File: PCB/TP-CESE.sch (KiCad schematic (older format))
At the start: 27 parts, among them J1 Conn_01x04_Female, J2 Conn_02x02_Odd_Even, Q1 IRF540N, Q2 IRF540N, Q3 IRF540N, Q4 IRF540N, U1 4N25, U2 4N25, U3 4N25, U4 4N25

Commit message: Agrego libreria poncho de edu-ciaa y hojas de datos
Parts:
- removed J1: Conn_01x04_Female, symbol Connector:Conn_01x04_Female
- removed J2: Conn_02x02_Odd_Even, Connector_PinSocket_2.54mm:PinSocket_2x02_P2.54mm_Vertical, symbol Connector_Generic:Conn_02x02_Odd_Even
- added J1: Screw_Terminal_01x04, symbol Connector:Screw_Terminal_01x04
- added J3: Screw_Terminal_01x02, symbol Connector:Screw_Terminal_01x02
- added XA? (x2): Conn_Poncho2P_2x_20x2, symbol Poncho_Esqueleto:Conn_Poncho2P_2x_20x2
- gave numbers to parts that had none: 1
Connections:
- wire segments 71 -> 87
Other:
- note added: "Alimentacion fuente de alimentacion\ndiferente de Edu-Ciaa \nTension de alimentacion: 5Volts /3 Amp\n"
- moved on the sheet: Q1, Q2, Q3, Q4, R1, R10, R11, R12, R13, R14, R15, R16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

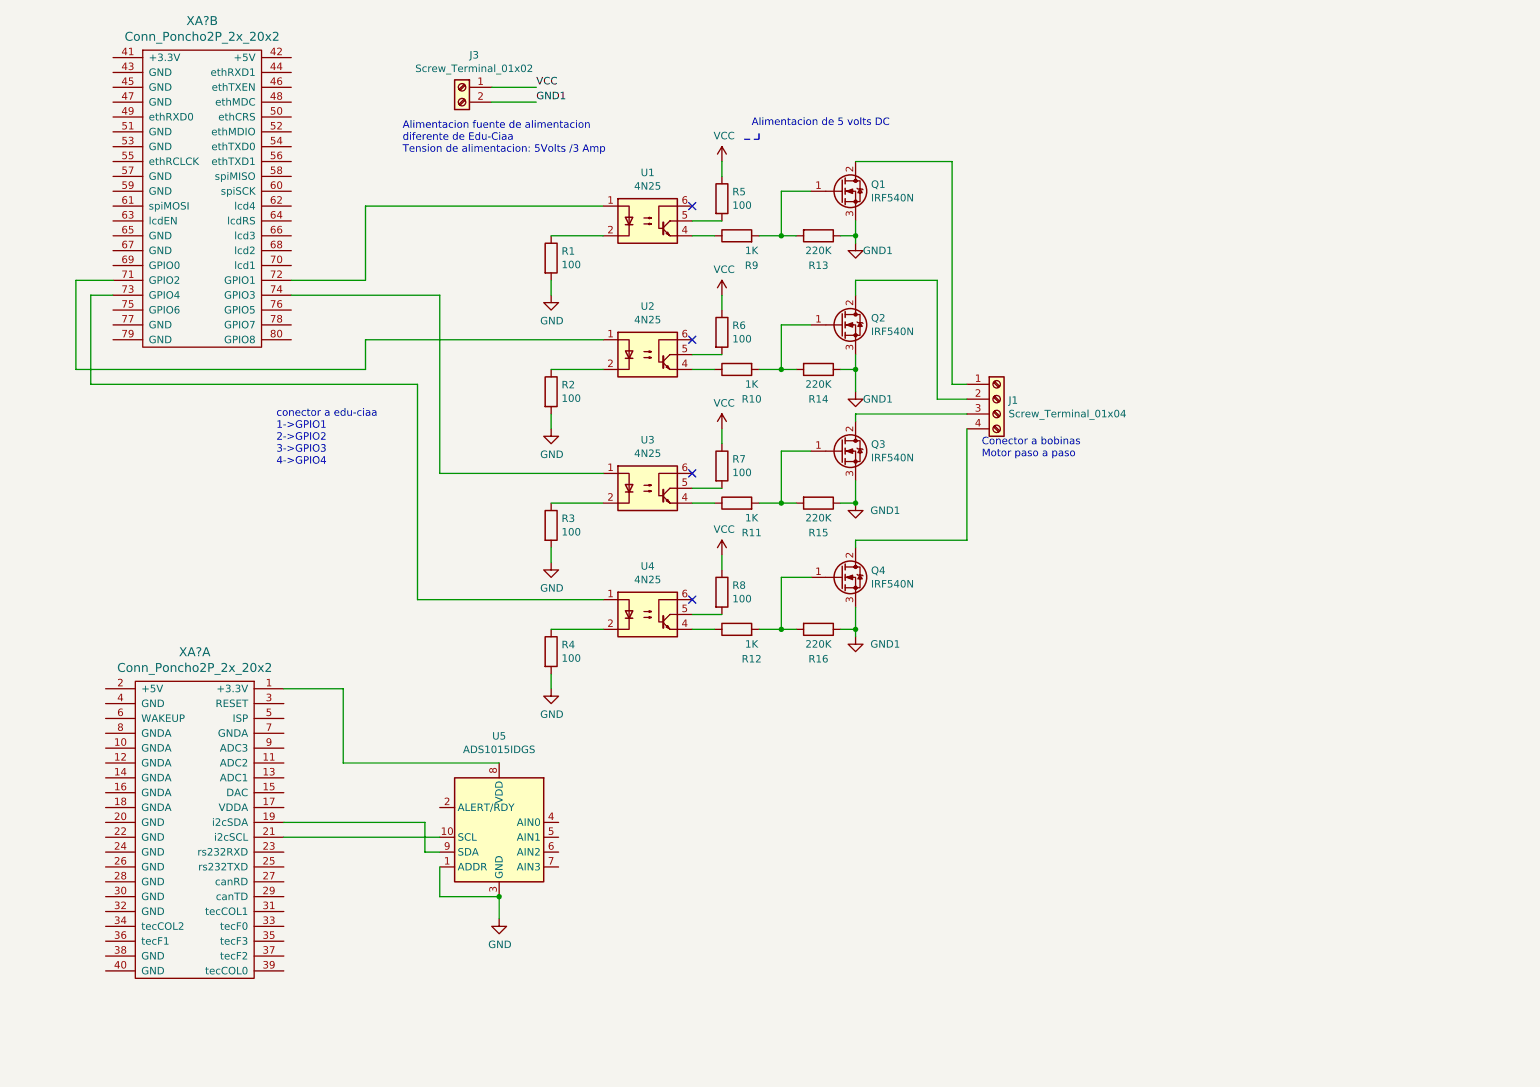
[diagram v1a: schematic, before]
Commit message: Conexiones, diodos de protecccion
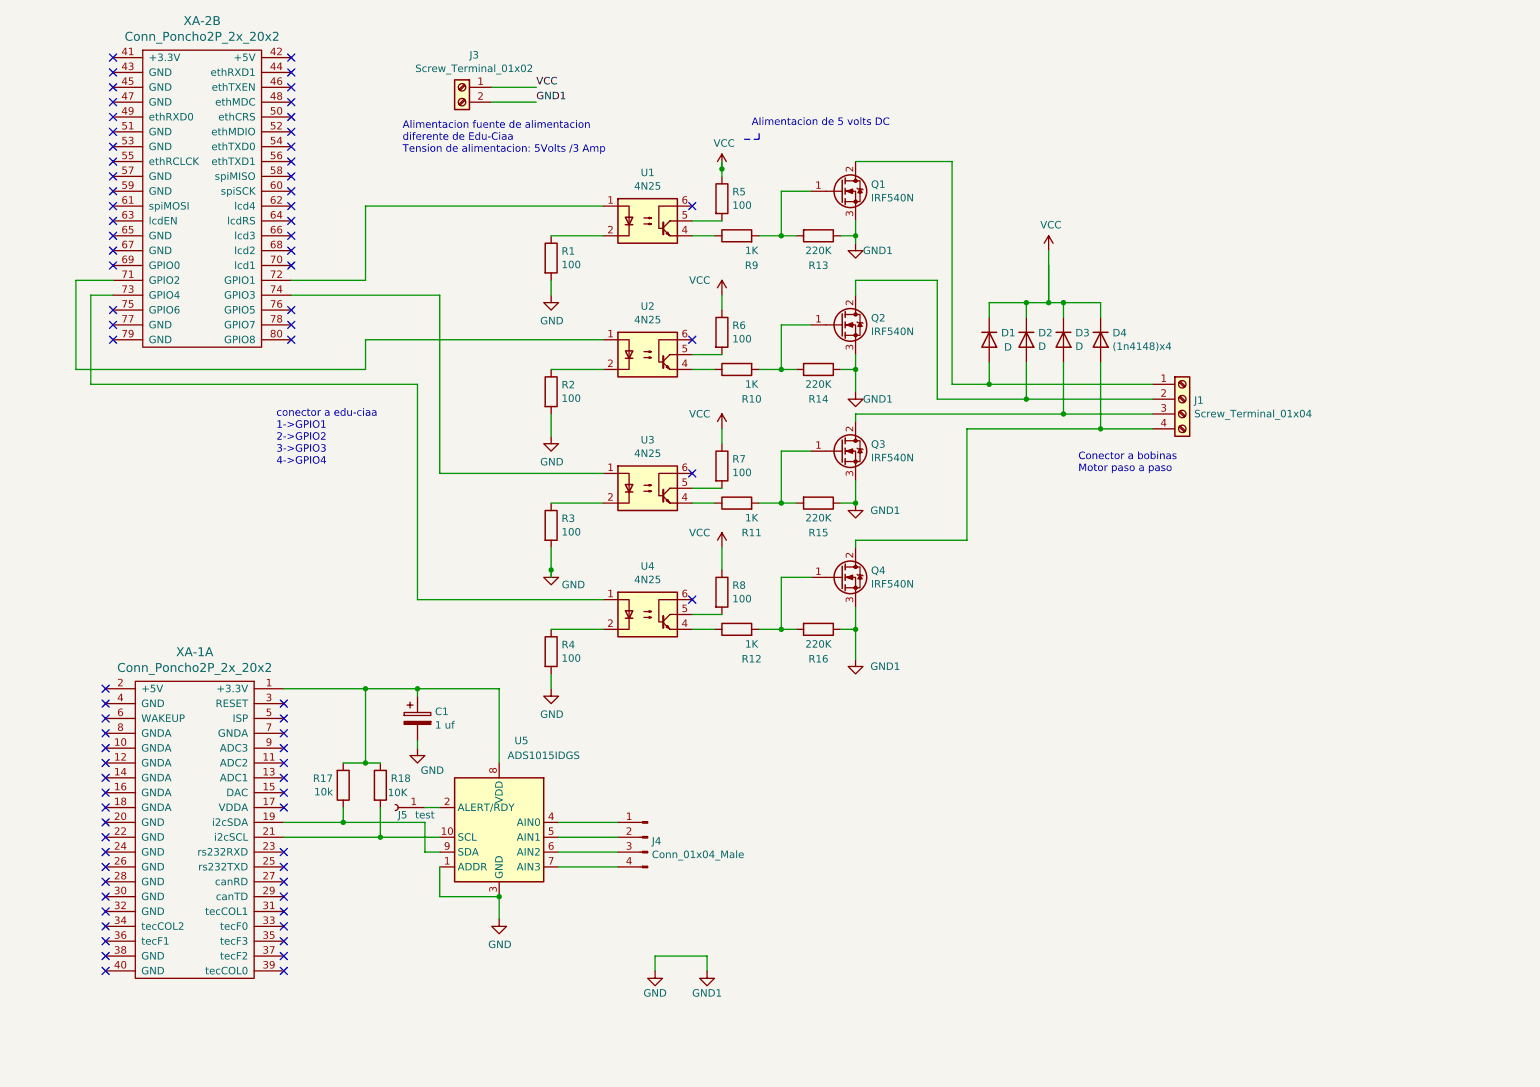
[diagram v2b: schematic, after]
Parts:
- added C1: 1 uf, symbol Device:CP
- added D1, D2, D3: D, symbol Device:D
- added D4: (1n4148)x4, symbol Device:D
- added J4: Conn_01x04_Male, symbol Connector:Conn_01x04_Male
- added J5: test, symbol Connector:Conn_01x01_Female
- added R17: 10k, symbol Device:R
- added R18: 10K, symbol Device:R
- gave numbers to parts that had none: 2
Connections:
- net GND1 is gone; now on net GND: J3.2 (Pin_2), Q1.3 (S), Q2.3 (S), Q3.3 (S), Q4.3 (S), R13.1, R14.1, R15.1, R16.1
- net GND: now also C1.2
- net VCC: now also D1.1 (K), D2.1 (K), D3.1 (K), D4.1 (K)
- net at J1.1 (Pin_1), Q1.2 (D): now also D1.2 (A)
- net at J1.2 (Pin_2), Q2.2 (D): now also D2.2 (A)
- net at J1.3 (Pin_3), Q3.2 (D): now also D3.2 (A)
- net at J1.4 (Pin_4), Q4.2 (D): now also D4.2 (A)
- net at U5.8 (VDD), XA-1.1 (+3.3V): now also C1.1, R17.2, R18.1
- net at U5.9 (SDA), XA-1.19 (i2cSDA): now also R17.1
- net at U5.10 (SCL), XA-1.21 (i2cSCL): now also R18.2
- net at U5.2 (ALERT/RDY): now also J5.1 (Pin_1)
- net at U5.4 (AIN0): now also J4.1 (Pin_1)
- net at U5.5 (AIN1): now also J4.2 (Pin_2)
- net at U5.6 (AIN2): now also J4.3 (Pin_3)
- net at U5.7 (AIN3): now also J4.4 (Pin_4)
- no-connect marks 4 -> 77
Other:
- moved on the sheet: J1

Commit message: agrego huellas, hojas de datos de diodo y tabla de potencia de resistencia smd
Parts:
- C1: footprint (none) -> Capacitor_SMD:CP_Elec_4x5.4
- D1, D2, D3, D4: footprint (none) -> Diode_THT:D_5W_P10.16mm_Horizontal
- J1: footprint (none) -> TerminalBlock_Phoenix:TerminalBlock_Phoenix_MKDS-1,5-4-5.08_1x04_P5.08mm_Horizontal
- J3: footprint (none) -> TerminalBlock_Phoenix:TerminalBlock_Phoenix_MKDS-1,5-2-5.08_1x02_P5.08mm_Horizontal
- J4: footprint (none) -> Connector_PinHeader_2.00mm:PinHeader_1x04_P2.00mm_Vertical
- J5: footprint (none) -> Connector_PinHeader_2.00mm:PinHeader_1x01_P2.00mm_Vertical
- Q1, Q2, Q3, Q4: footprint Package_TO_SOT_THT:TO-220-3_Vertical -> Package_TO_SOT_THT:TO-262-3_Vertical
- R1, R2, R3, R4: footprint (none) -> Resistor_SMD:R_2010_5025Metric_Pad1.52x2.65mm_HandSolder
- R10, R11, R12, R5, R6, R7, R8, R9: footprint (none) -> Resistor_SMD:R_2512_6332Metric_Pad1.52x3.35mm_HandSolder
- R13, R14, R15, R16, R17, R18: footprint (none) -> Resistor_SMD:R_1210_3225Metric
- XA-1, XA-2: footprint (none) -> Poncho_Esqueleto:Conn_Poncho_Chico
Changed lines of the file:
@@
 F 0 "R1" H 4320 2196 50  0000 L CNN
 F 1 "100" H 4320 2105 50  0000 L CNN
-F 2 "" V 4180 2150 50  0001 C CNN
+F 2 "Resistor_SMD:R_2010_5025Metric_Pad1.52x2.65mm_HandSolder" V 4180 2150 50  0001 C CNN
 F 3 "~" H 4250 2150 50  0001 C CNN
 	1    4250 2150
@@
 F 0 "R2" H 4320 3096 50  0000 L CNN
 F 1 "100" H 4320 3005 50  0000 L CNN
-F 2 "" V 4180 3050 50  0001 C CNN
+F 2 "Resistor_SMD:R_2010_5025Metric_Pad1.52x2.65mm_HandSolder" V 4180 3050 50  0001 C CNN
 F 3 "~" H 4250 3050 50  0001 C CNN
 	1    4250 3050
@@
 F 0 "R3" H 4320 3996 50  0000 L CNN
 F 1 "100" H 4320 3905 50  0000 L CNN
-F 2 "" V 4180 3950 50  0001 C CNN
+F 2 "Resistor_SMD:R_2010_5025Metric_Pad1.52x2.65mm_HandSolder" V 4180 3950 50  0001 C CNN
 F 3 "~" H 4250 3950 50  0001 C CNN
 	1    4250 3950
@@
 F 0 "R4" H 4320 4846 50  0000 L CNN
 F 1 "100" H 4320 4755 50  0000 L CNN
-F 2 "" V 4180 4800 50  0001 C CNN
+F 2 "Resistor_SMD:R_2010_5025Metric_Pad1.52x2.65mm_HandSolder" V 4180 4800 50  0001 C CNN
 F 3 "~" H 4250 4800 50  0001 C CNN
 	1    4250 4800
@@
 F 0 "R5" H 5470 1796 50  0000 L CNN
 F 1 "100" H 5470 1705 50  0000 L CNN
-F 2 "" V 5330 1750 50  0001 C CNN
+F 2 "Resistor_SMD:R_2512_6332Metric_Pad1.52x3.35mm_HandSolder" V 5330 1750 50  0001 C CNN
 F 3 "~" H 5400 1750 50  0001 C CNN
 	1    5400 1750
@@
 F 0 "R6" H 5470 2696 50  0000 L CNN
 F 1 "100" H 5470 2605 50  0000 L CNN
-F 2 "" V 5330 2650 50  0001 C CNN
+F 2 "Resistor_SMD:R_2512_6332Metric_Pad1.52x3.35mm_HandSolder" V 5330 2650 50  0001 C CNN
 F 3 "~" H 5400 2650 50  0001 C CNN
 	1    5400 2650
@@
 F 0 "R7" H 5470 3596 50  0000 L CNN
 F 1 "100" H 5470 3505 50  0000 L CNN
-F 2 "" V 5330 3550 50  0001 C CNN
+F 2 "Resistor_SMD:R_2512_6332Metric_Pad1.52x3.35mm_HandSolder" V 5330 3550 50  0001 C CNN
 F 3 "~" H 5400 3550 50  0001 C CNN
 	1    5400 3550
@@
 F 0 "R8" H 5470 4446 50  0000 L CNN
 F 1 "100" H 5470 4355 50  0000 L CNN
-F 2 "" V 5330 4400 50  0001 C CNN
+F 2 "Resistor_SMD:R_2512_6332Metric_Pad1.52x3.35mm_HandSolder" V 5330 4400 50  0001 C CNN
 F 3 "~" H 5400 4400 50  0001 C CNN
 	1    5400 4400
@@
 F 0 "R9" V 5300 1900 50  0000 C CNN
 F 1 "1K" V 5400 1900 50  0000 C CNN
-F 2 "" V 5430 2000 50  0001 C CNN
+F 2 "Resistor_SMD:R_2512_6332Metric_Pad1.52x3.35mm_HandSolder" V 5430 2000 50  0001 C CNN
 F 3 "~" H 5500 2000 50  0001 C CNN
 	1    5500 2000
@@
 F 0 "R10" V 5700 2800 50  0000 C CNN
 F 1 "1K" V 5600 2800 50  0000 C CNN
-F 2 "" V 5430 2900 50  0001 C CNN
+F 2 "Resistor_SMD:R_2512_6332Metric_Pad1.52x3.35mm_HandSolder" V 5430 2900 50  0001 C CNN
 F 3 "~" H 5500 2900 50  0001 C CNN
 	1    5500 2900
@@
 F 0 "R11" V 5300 3700 50  0000 C CNN
 F 1 "1K" V 5400 3700 50  0000 C CNN
-F 2 "" V 5430 3800 50  0001 C CNN
+F 2 "Resistor_SMD:R_2512_6332Metric_Pad1.52x3.35mm_HandSolder" V 5430 3800 50  0001 C CNN
 F 3 "~" H 5500 3800 50  0001 C CNN
 	1    5500 3800
@@
 F 0 "R12" V 5300 4550 50  0000 C CNN
 F 1 "1K" V 5400 4550 50  0000 C CNN
-F 2 "" V 5430 4650 50  0001 C CNN
+F 2 "Resistor_SMD:R_2512_6332Metric_Pad1.52x3.35mm_HandSolder" V 5430 4650 50  0001 C CNN
 F 3 "~" H 5500 4650 50  0001 C CNN
 	1    5500 4650
@@
 F 0 "R13" V 6250 2000 50  0000 C CNN
 F 1 "220K" V 6150 2000 50  0000 C CNN
-F 2 "" V 5980 2000 50  0001 C CNN
+F 2 "Resistor_SMD:R_1210_3225Metric" V 5980 2000 50  0001 C CNN
 F 3 "~" H 6050 2000 50  0001 C CNN
 	1    6050 2000
@@
 F 0 "R14" V 6250 2900 50  0000 C CNN
 F 1 "220K" V 6150 2900 50  0000 C CNN
-F 2 "" V 5980 2900 50  0001 C CNN
+F 2 "Resistor_SMD:R_1210_3225Metric" V 5980 2900 50  0001 C CNN
 F 3 "~" H 6050 2900 50  0001 C CNN
 	1    6050 2900
@@
 F 0 "R15" V 6250 3800 50  0000 C CNN
 F 1 "220K" V 6150 3800 50  0000 C CNN
-F 2 "" V 5980 3800 50  0001 C CNN
+F 2 "Resistor_SMD:R_1210_3225Metric" V 5980 3800 50  0001 C CNN
 F 3 "~" H 6050 3800 50  0001 C CNN
 	1    6050 3800
@@
 F 0 "R16" V 6250 4650 50  0000 C CNN
 F 1 "220K" V 6150 4650 50  0000 C CNN
-F 2 "" V 5980 4650 50  0001 C CNN
+F 2 "Resistor_SMD:R_1210_3225Metric" V 5980 4650 50  0001 C CNN
 F 3 "~" H 6050 4650 50  0001 C CNN
 	1    6050 4650
@@
 F 0 "Q1" H 6404 1746 50  0000 L CNN
 F 1 "IRF540N" H 6404 1655 50  0000 L CNN
-F 2 "Package_TO_SOT_THT:TO-220-3_Vertical" H 6450 1625 50  0001 L CIN
+F 2 "Package_TO_SOT_THT:TO-262-3_Vertical" H 6450 1625 50  0001 L CIN
 F 3 "http://www.irf.com/product-info/datasheets/data/irf540n.pdf" H 6200 1700 50  0001 L CNN
 	1    6200 1700
@@
 F 0 "Q2" H 6404 2646 50  0000 L CNN
 F 1 "IRF540N" H 6404 2555 50  0000 L CNN
-F 2 "Package_TO_SOT_THT:TO-220-3_Vertical" H 6450 2525 50  0001 L CIN
+F 2 "Package_TO_SOT_THT:TO-262-3_Vertical" H 6450 2525 50  0001 L CIN
 F 3 "http://www.irf.com/product-info/datasheets/data/irf540n.pdf" H 6200 2600 50  0001 L CNN
 	1    6200 2600
@@
 F 0 "Q3" H 6404 3496 50  0000 L CNN
 F 1 "IRF540N" H 6404 3405 50  0000 L CNN
-F 2 "Package_TO_SOT_THT:TO-220-3_Vertical" H 6450 3375 50  0001 L CIN
+F 2 "Package_TO_SOT_THT:TO-262-3_Vertical" H 6450 3375 50  0001 L CIN
 F 3 "http://www.irf.com/product-info/datasheets/data/irf540n.pdf" H 6200 3450 50  0001 L CNN
 	1    6200 3450
@@
 F 0 "Q4" H 6404 4346 50  0000 L CNN
 F 1 "IRF540N" H 6404 4255 50  0000 L CNN
-F 2 "Package_TO_SOT_THT:TO-220-3_Vertical" H 6450 4225 50  0001 L CIN
+F 2 "Package_TO_SOT_THT:TO-262-3_Vertical" H 6450 4225 50  0001 L CIN
 F 3 "http://www.irf.com/product-info/datasheets/data/irf540n.pdf" H 6200 4300 50  0001 L CNN
 	1    6200 4300
@@
 NoConn ~ 5200 2700
 NoConn ~ 5200 1800
-Text Notes 5600 1350 0    50   ~ 0
-Alimentacion de 5 volts DC \n\n
 Wire Notes Line
 	5550 1350 5650 1350
 Wire Notes Line
 	5650 1350 5650 1300
-Wire Wire Line
-	6300 1500 6950 1500
-Wire Wire Line
-	6950 1500 6950 3000
 Wire Wire Line
 	6300 2400 6300 2300
@@
 F 0 "J1" H 8580 3092 50  0000 L CNN
 F 1 "Screw_Terminal_01x04" H 8580 3001 50  0000 L CNN
-F 2 "" H 8500 3100 50  0001 C CNN
+F 2 "TerminalBlock_Phoenix:TerminalBlock_Phoenix_MKDS-1,5-4-5.08_1x04_P5.08mm_Horizontal" H 8500 3100 50  0001 C CNN
 F 3 "~" H 8500 3100 50  0001 C CNN
 	1    8500 3100
@@
 F 0 "J3" H 3568 1217 50  0000 C CNN
 F 1 "Screw_Terminal_01x02" H 3568 1126 50  0000 C CNN
-F 2 "" H 3650 1000 50  0001 C CNN
+F 2 "TerminalBlock_Phoenix:TerminalBlock_Phoenix_MKDS-1,5-2-5.08_1x02_P5.08mm_Horizontal" H 3650 1000 50  0001 C CNN
 F 3 "~" H 3650 1000 50  0001 C CNN
 	1    3650 1000
@@
 F 0 "XA-2" H 1900 1647 60  0000 C CNN
 F 1 "Conn_Poncho2P_2x_20x2" H 1900 1541 60  0000 C CNN
-F 2 "" H 1550 1100 60  0000 C CNN
+F 2 "Poncho_Esqueleto:Conn_Poncho_Chico" H 1550 1100 60  0001 C CNN
 F 3 "" H 1550 1100 60  0000 C CNN
 	2    1550 1100
@@
 F 0 "XA-1" H 2550 5897 60  0000 C CNN
 F 1 "Conn_Poncho2P_2x_20x2" H 2550 5791 60  0000 C CNN
-F 2 "" H 2200 5350 60  0000 C CNN
+F 2 "Poncho_Esqueleto:Conn_Poncho_Chico" H 2200 5350 60  0001 C CNN
 F 3 "" H 2200 5350 60  0000 C CNN
 	1    2200 5350
@@
 F 0 "C1" H 3468 5296 50  0000 L CNN
 F 1 "1 uf" H 3468 5205 50  0000 L CNN
-F 2 "" H 3388 5100 50  0001 C CNN
+F 2 "Capacitor_SMD:CP_Elec_4x5.4" H 3388 5100 50  0001 C CNN
 F 3 "~" H 3350 5250 50  0001 C CNN
 	1    3350 5250
@@
 F 0 "R17" H 2781 5654 50  0000 R CNN
 F 1 "10k" H 2781 5745 50  0000 R CNN
-F 2 "" V 2780 5700 50  0001 C CNN
+F 2 "Resistor_SMD:R_1210_3225Metric" V 2780 5700 50  0001 C CNN
 F 3 "~" H 2850 5700 50  0001 C CNN
 	1    2850 5700
@@
 F 0 "R18" H 3170 5746 50  0000 L CNN
 F 1 "10K" H 3150 5650 50  0000 L CNN
-F 2 "" V 3030 5700 50  0001 C CNN
+F 2 "Resistor_SMD:R_1210_3225Metric" V 3030 5700 50  0001 C CNN
 F 3 "~" H 3100 5700 50  0001 C CNN
 	1    3100 5700
@@
 F 0 "J4" H 4872 6024 50  0000 R CNN
 F 1 "Conn_01x04_Male" H 4872 5933 50  0000 R CNN
-F 2 "" H 4900 6050 50  0001 C CNN
+F 2 "Connector_PinHeader_2.00mm:PinHeader_1x04_P2.00mm_Vertical" H 4900 6050 50  0001 C CNN
 F 3 "~" H 4900 6050 50  0001 C CNN
 	1    4900 6050
@@
 F 0 "J5" H 3150 5800 50  0000 C CNN
 F 1 "test" H 3000 5800 50  0000 C CNN
-F 2 "" H 3200 5850 50  0001 C CNN
+F 2 "Connector_PinHeader_2.00mm:PinHeader_1x01_P2.00mm_Vertical" H 3200 5850 50  0001 C CNN
 F 3 "~" H 3200 5850 50  0001 C CNN
 	1    3200 5850
@@
 F 0 "D1" V 7154 2780 50  0000 L CNN
 F 1 "D" V 7250 2800 50  0000 L CNN
-F 2 "" H 7200 2700 50  0001 C CNN
+F 2 "Diode_THT:D_5W_P10.16mm_Horizontal" H 7200 2700 50  0001 C CNN
 F 3 "~" H 7200 2700 50  0001 C CNN
 	1    7200 2700
@@
 F 0 "D2" V 7404 2780 50  0000 L CNN
 F 1 "D" V 7495 2780 50  0000 L CNN
-F 2 "" H 7450 2700 50  0001 C CNN
+F 2 "Diode_THT:D_5W_P10.16mm_Horizontal" H 7450 2700 50  0001 C CNN
 F 3 "~" H 7450 2700 50  0001 C CNN
 	1    7450 2700
@@
 F 0 "D3" V 7654 2780 50  0000 L CNN
 F 1 "D" V 7745 2780 50  0000 L CNN
-F 2 "" H 7700 2700 50  0001 C CNN
+F 2 "Diode_THT:D_5W_P10.16mm_Horizontal" H 7700 2700 50  0001 C CNN
 F 3 "~" H 7700 2700 50  0001 C CNN
 	1    7700 2700
@@
 F 0 "D4" V 7904 2780 50  0000 L CNN
 F 1 "(1n4148)x4" V 7995 2780 50  0000 L CNN
-F 2 "" H 7950 2700 50  0001 C CNN
+F 2 "Diode_THT:D_5W_P10.16mm_Horizontal" H 7950 2700 50  0001 C CNN
 F 3 "~" H 7950 2700 50  0001 C CNN
 	1    7950 2700
@@
 Wire Wire Line
 	7700 3200 8300 3200
-Wire Wire Line
-	7950 2850 7950 3300
 Connection ~ 7950 3300
 Wire Wire Line
@@
 Wire Wire Line
 	5400 1550 5400 1600
+Wire Wire Line
+	7950 2850 7950 3300
+Wire Wire Line
+	6950 1500 6950 3000
+Wire Wire Line
+	6300 1500 6950 1500
+Text Notes 5600 1350 0    50   ~ 0
+Alimentacion de 5 volts DC \n\n
 $EndSCHEMATC
